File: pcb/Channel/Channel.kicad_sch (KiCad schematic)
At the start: 11 parts, among them J1 Mainboard, J2 SPI_CHAIN_IN, J3 SPI_CHAIN_OUT, J4 Motor_Out, J6 Motor_In, SW1 RotaryEncoder_Switch

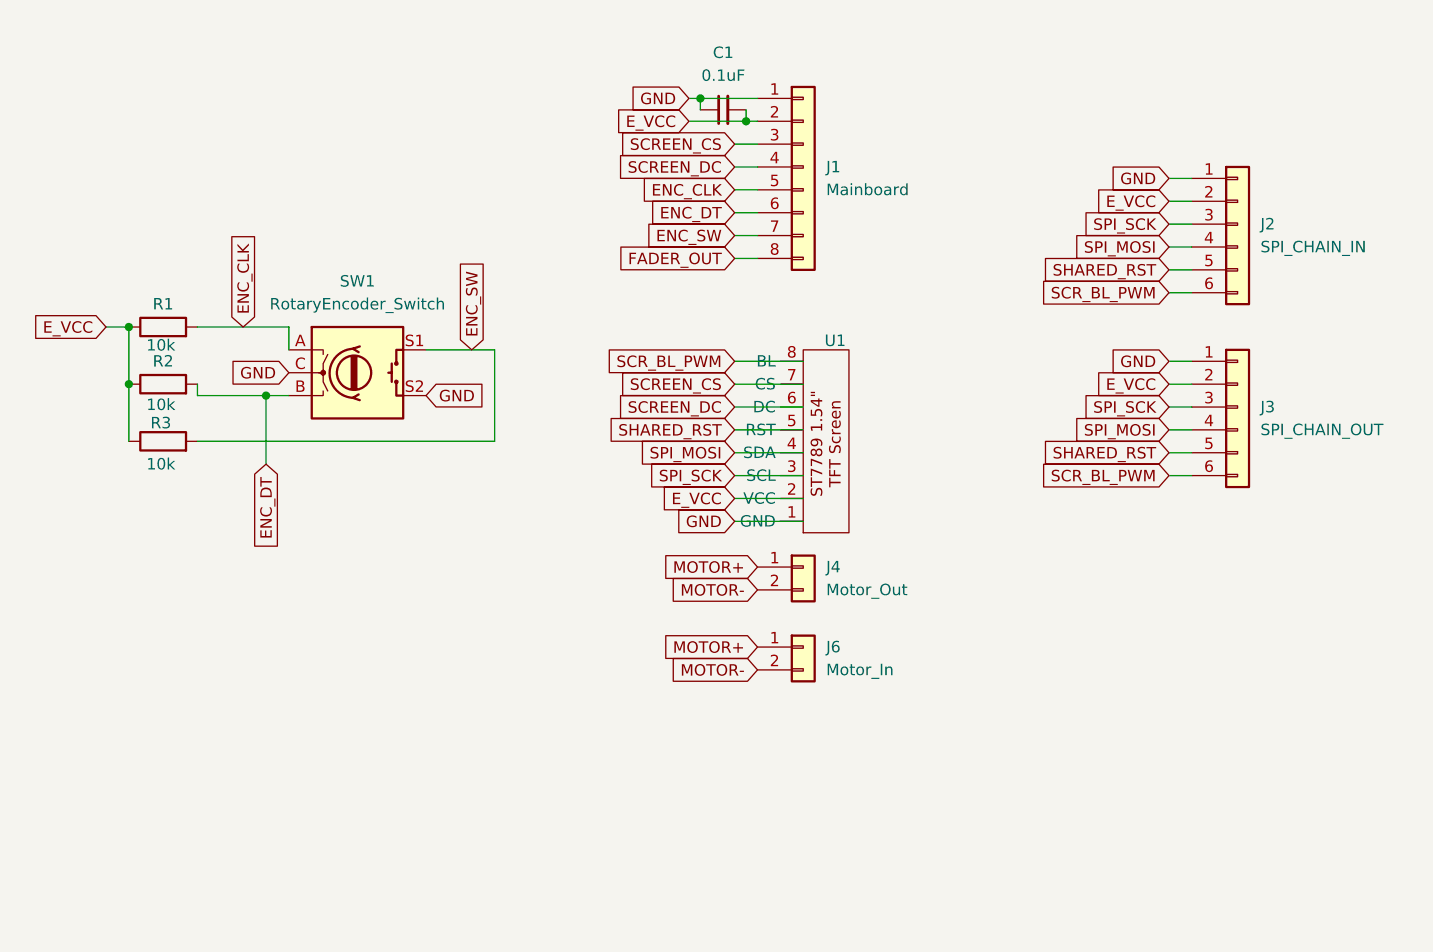
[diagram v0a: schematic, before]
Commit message: Update main pcb silkscreen.
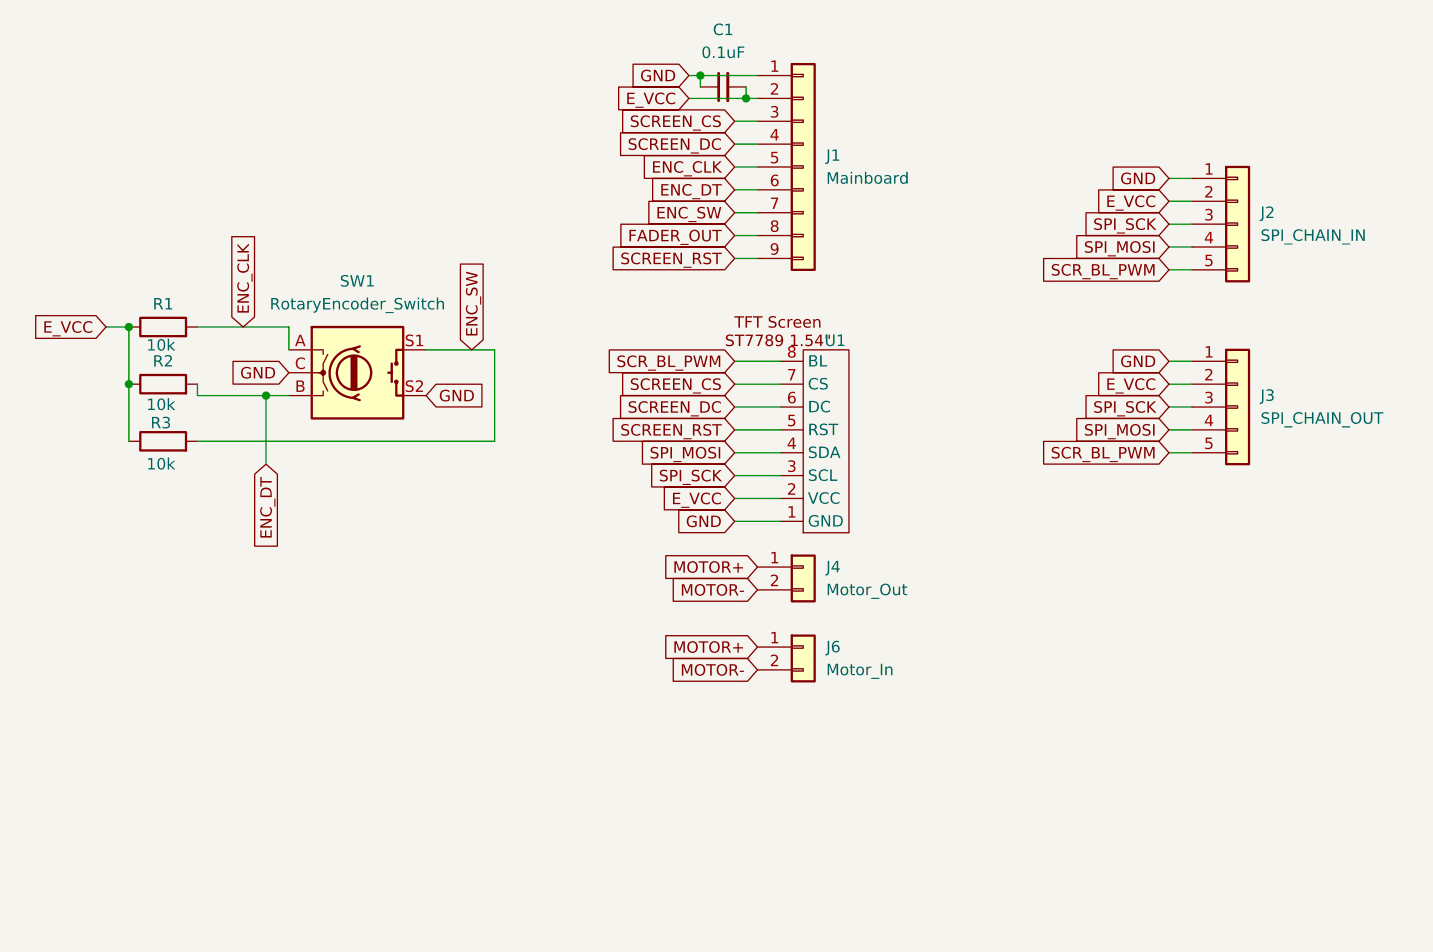
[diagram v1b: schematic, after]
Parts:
- J1: footprint Connector_PinSocket_2.00mm:PinSocket_1x08_P2.00mm_Vertical -> Connector_PinSocket_2.00mm:PinSocket_1x09_P2.00mm_Vertical; symbol Connector_Generic:Conn_01x08 -> Connector_Generic:Conn_01x09
- J2, J3: footprint Connector_PinSocket_2.00mm:PinSocket_1x06_P2.00mm_Vertical -> Connector_PinSocket_2.00mm:PinSocket_1x05_P2.00mm_Vertical; symbol Connector_Generic:Conn_01x06 -> Connector_Generic:Conn_01x05
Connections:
- net SCR_BL_PWM: now also J2.5 (Pin_5), J3.5 (Pin_5); no longer J2.6 (Pin_6), J3.6 (Pin_6)
- removed net SHARED_RST: J2.5 (Pin_5), J3.5 (Pin_5), U1.5 (RST)
- new net SCREEN_RST: J1.9 (Pin_9), U1.5 (RST)
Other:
- moved on the sheet: C1, U1

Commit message: Fix up channel pcb
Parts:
- added F1: ~, Behringer X32 Fader:Behringer X32 Fader, symbol Behringer X32 Fader:Fader_Motorized_100mm
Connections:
- net E_VCC: now also F1.3 (T2)
- net FADER_OUT: now also F1.2 (W)
- net GND: now also F1.1 (T1)
- net MOTOR+: now also F1. (M+)
- net MOTOR-: now also F1. (M+)
